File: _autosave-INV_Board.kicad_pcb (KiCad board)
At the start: 4 copper layers, 84 x 66.5 mm, 194 parts, among them J3 Conn_01x06_Male, J4 Conn_01x06_Female, J5 Conn_01x08_Female, J6 Conn_01x08_Female, J7 Conn_01x05_Male, J8 Conn_01x02_Male, Q1 2N7002, Q2 AO3401A, Q3 CRSS037N10N, Q4 CRSS037N10N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

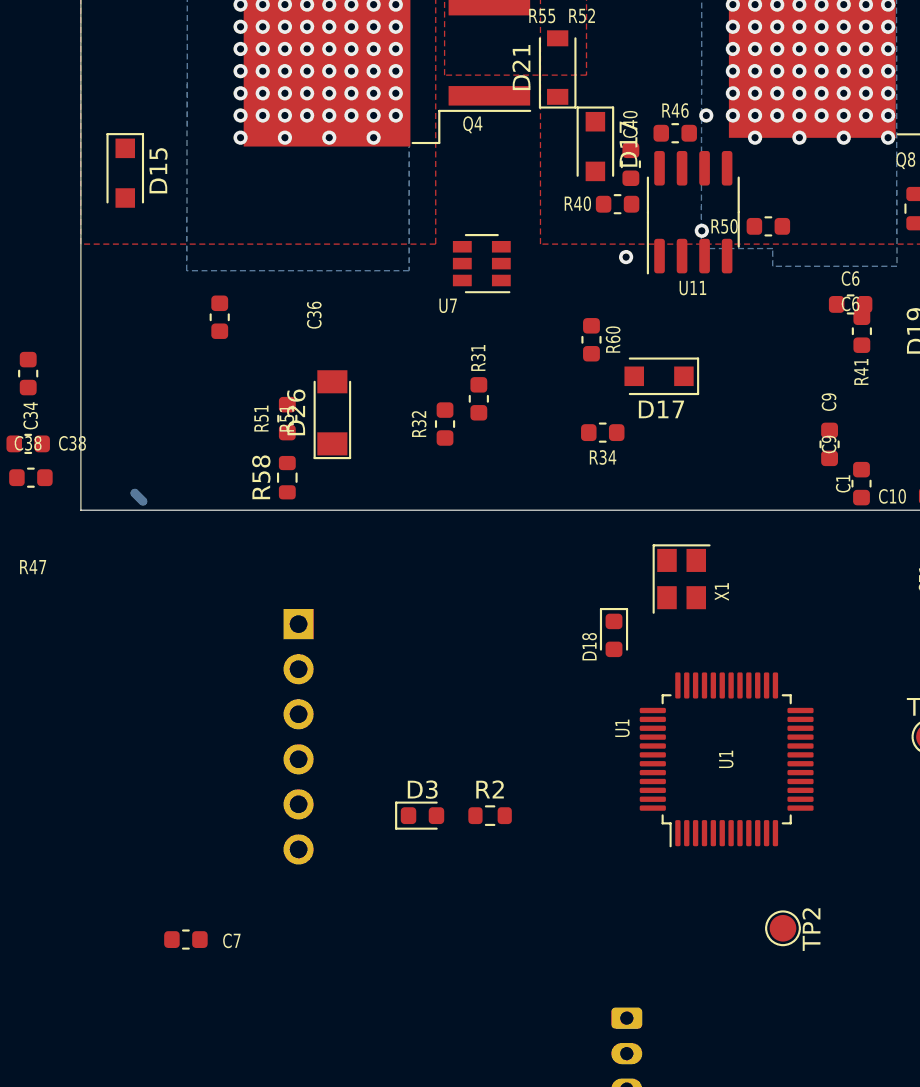
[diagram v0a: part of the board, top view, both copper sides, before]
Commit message: Checkpoint before deleting MCU ISense
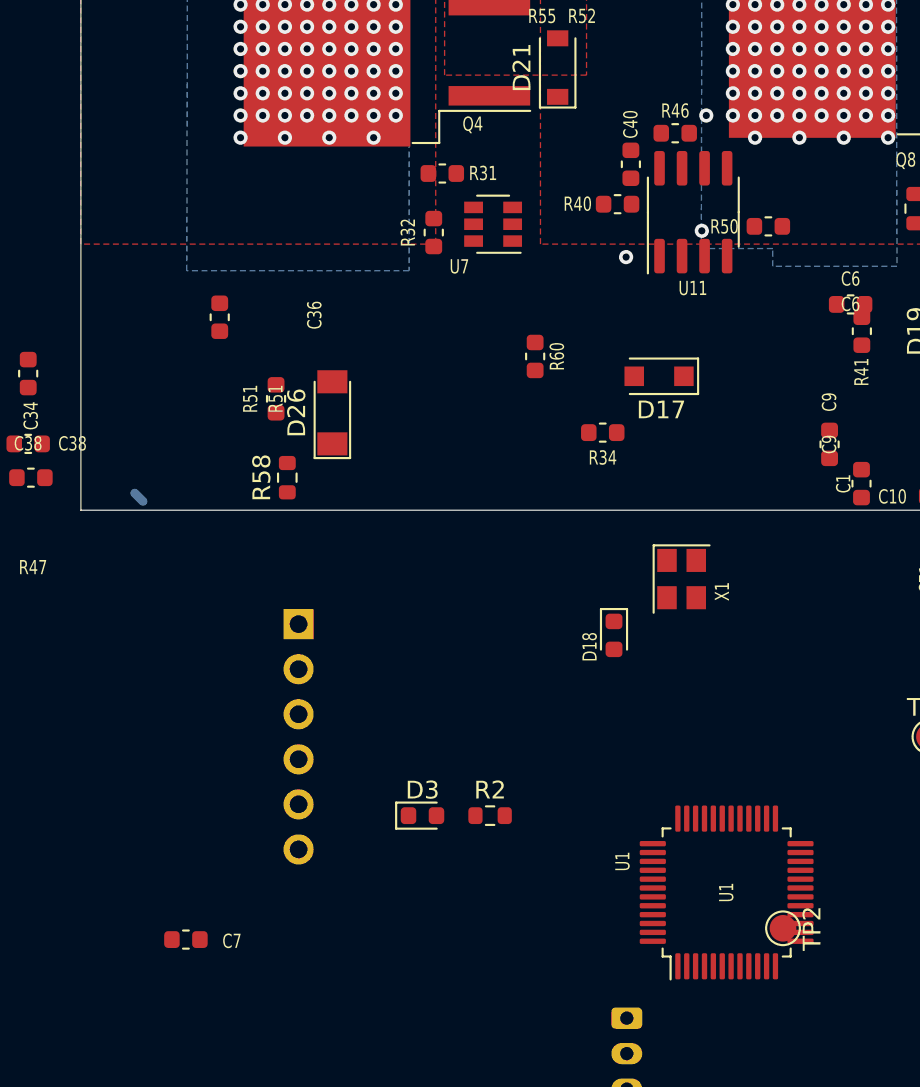
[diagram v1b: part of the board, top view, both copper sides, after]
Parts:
- removed the D15 at (118.5, 96.5)
- removed the D17 at (145.0, 95.0)
- moved R31 12.9 mm to (136.4, 96.5), turned to 0 degrees
- moved R32 10.8 mm to (135.9, 99.8)
- moved U1 7.50 mm to (152.4, 137.0)
- moved R60 3.31 mm to (141.6, 106.8)
- moved U7 2.31 mm to (139.2, 99.4)
- moved R51 1.29 mm to (127.0, 109.2)
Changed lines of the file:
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@@
   )
   (footprint "Package_QFP:LQFP-48_7x7mm_P0.5mm" (layer "F.Cu")
-    (at 152.4 129.54 90)
+    (at 152.4 137.045 90)
     (descr "LQFP, 48 Pin (https://www.analog.com/media/en/technical-documentation/data-sheets/ltc2358-16.pdf), generated with kicad-footprint-generator ipc_gullwing_generator.py")
     (tags "LQFP QFP")
@@
     )
   )
-  (footprint "Diode_SMD:D_SOD-123F" (layer "F.Cu")
-    (at 145 95 -90)
-    (descr "D_SOD-123F")
-    (tags "D_SOD-123F")
-    (property "LCSC" "C64898")
-    (property "Mouser Part no." "")
-    (property "MouserAlt" "")
-    (property "Sheetfile" "/Users/user/Documents/Git/my_MESC/INV_Board.sch")
-    (property "Sheetname" "")
-    (attr smd)
-    (fp_text reference "D17" (at -0.127 -1.905 -90) (layer "F.SilkS")
-      (effects (font (size 1 1) (thickness 0.15)))
-    )
-    (fp_text value "D_Sch_100V_2A" (at 0 2.1 -90) (layer "F.Fab")
-      (effects (font (size 1 1) (thickness 0.15)))
-    )
-    (fp_text user "${REFERENCE}" (at -0.127 -1.905 -90) (layer "F.Fab")
-      (effects (font (size 1 1) (thickness 0.15)))
-    )
-    (fp_line (start -2.2 1) (end 1.65 1) (layer "F.SilkS") (width 0.12))
-    (fp_line (start -2.2 -1) (end -2.2 1) (layer "F.SilkS") (width 0.12))
-    (fp_line (start -2.2 -1) (end 1.65 -1) (layer "F.SilkS") (width 0.12))
-    (fp_line (start 2.2 1.15) (end -2.2 1.15) (layer "F.CrtYd") (width 0.05))
-    (fp_line (start 2.2 -1.15) (end 2.2 1.15) (layer "F.CrtYd") (width 0.05))
-    (fp_line (start -2.2 -1.15) (end 2.2 -1.15) (layer "F.CrtYd") (width 0.05))
-    (fp_line (start -2.2 -1.15) (end -2.2 1.15) (layer "F.CrtYd") (width 0.05))
-    (fp_line (start -0.35 0) (end -0.35 0.55) (layer "F.Fab") (width 0.1))
-    (fp_line (start -0.35 0) (end -0.35 -0.55) (layer "F.Fab") (width 0.1))
-    (fp_line (start 1.4 -0.9) (end 1.4 0.9) (layer "F.Fab") (width 0.1))
-    (fp_line (start 0.25 -0.4) (end 0.25 0.4) (layer "F.Fab") (width 0.1))
-    (fp_line (start -1.4 -0.9) (end 1.4 -0.9) (layer "F.Fab") (width 0.1))
-    (fp_line (start 1.4 0.9) (end -1.4 0.9) (layer "F.Fab") (width 0.1))
-    (fp_line (start 0.25 0.4) (end -0.35 0) (layer "F.Fab") (width 0.1))
-    (fp_line (start -0.75 0) (end -0.35 0) (layer "F.Fab") (width 0.1))
-    (fp_line (start -0.35 0) (end 0.25 -0.4) (layer "F.Fab") (width 0.1))
-    (fp_line (start -1.4 0.9) (end -1.4 -0.9) (layer "F.Fab") (width 0.1))
-    (fp_line (start 0.25 0) (end 0.75 0) (layer "F.Fab") (width 0.1))
-    (pad "1" smd rect (at -1.4 0 270) (size 1.1 1.1) (layers "F.Cu" "F.Paste" "F.Mask")
-      (net 52 "Net-(C40-Pad1)") (pinfunction "K") (pintype "passive"))
-    (pad "2" smd rect (at 1.4 0 270) (size 1.1 1.1) (layers "F.Cu" "F.Paste" "F.Mask")
-      (net 62 "Net-(D17-Pad2)") (pinfunction "A") (pintype "passive"))
-    (model "${KICAD6_3DMODEL_DIR}/Diode_SMD.3dshapes/D_SOD-123F.wrl"
-      (offset (xyz 0 0 0))
-      (scale (xyz 1 1 1))
-      (rotate (xyz 0 0 0))
-    )
-  )
-  (footprint "Diode_SMD:D_SOD-123F" (layer "F.Cu")
-    (at 118.5 96.5 -90)
-    (descr "D_SOD-123F")
-    (tags "D_SOD-123F")
-    (property "LCSC" "C64898")
-    (property "Mouser Part no." "")
-    (property "MouserAlt" "")
-    (property "Sheetfile" "/Users/user/Documents/Git/my_MESC/INV_Board.sch")
-    (property "Sheetname" "")
-    (attr smd)
-    (fp_text reference "D15" (at -0.127 -1.905 -90) (layer "F.SilkS")
-      (effects (font (size 1 1) (thickness 0.15)))
-    )
-    (fp_text value "D_Sch_100V_2A" (at 0 2.1 -90) (layer "F.Fab")
-      (effects (font (size 1 1) (thickness 0.15)))
-    )
-    (fp_text user "${REFERENCE}" (at -0.127 -1.905 -90) (layer "F.Fab")
-      (effects (font (size 1 1) (thickness 0.15)))
-    )
-    (fp_line (start -2.2 -1) (end 1.65 -1) (layer "F.SilkS") (width 0.12))
-    (fp_line (start -2.2 -1) (end -2.2 1) (layer "F.SilkS") (width 0.12))
-    (fp_line (start -2.2 1) (end 1.65 1) (layer "F.SilkS") (width 0.12))
-    (fp_line (start -2.2 -1.15) (end 2.2 -1.15) (layer "F.CrtYd") (width 0.05))
-    (fp_line (start -2.2 -1.15) (end -2.2 1.15) (layer "F.CrtYd") (width 0.05))
-    (fp_line (start 2.2 1.15) (end -2.2 1.15) (layer "F.CrtYd") (width 0.05))
-    (fp_line (start 2.2 -1.15) (end 2.2 1.15) (layer "F.CrtYd") (width 0.05))
-    (fp_line (start 0.25 -0.4) (end 0.25 0.4) (layer "F.Fab") (width 0.1))
-    (fp_line (start -1.4 0.9) (end -1.4 -0.9) (layer "F.Fab") (width 0.1))
-    (fp_line (start 0.25 0.4) (end -0.35 0) (layer "F.Fab") (width 0.1))
-    (fp_line (start -0.35 0) (end 0.25 -0.4) (layer "F.Fab") (width 0.1))
-    (fp_line (start -1.4 -0.9) (end 1.4 -0.9) (layer "F.Fab") (width 0.1))
-    (fp_line (start -0.35 0) (end -0.35 0.55) (layer "F.Fab") (width 0.1))
-    (fp_line (start 1.4 0.9) (end -1.4 0.9) (layer "F.Fab") (width 0.1))
-    (fp_line (start -0.35 0) (end -0.35 -0.55) (layer "F.Fab") (width 0.1))
-    (fp_line (start 1.4 -0.9) (end 1.4 0.9) (layer "F.Fab") (width 0.1))
-    (fp_line (start -0.75 0) (end -0.35 0) (layer "F.Fab") (width 0.1))
-    (fp_line (start 0.25 0) (end 0.75 0) (layer "F.Fab") (width 0.1))
-    (pad "1" smd rect (at -1.4 0 270) (size 1.1 1.1) (layers "F.Cu" "F.Paste" "F.Mask")
-      (net 45 "Net-(C38-Pad1)") (pinfunction "K") (pintype "passive"))
-    (pad "2" smd rect (at 1.4 0 270) (size 1.1 1.1) (layers "F.Cu" "F.Paste" "F.Mask")
-      (net 60 "Net-(D15-Pad2)") (pinfunction "A") (pintype "passive"))
-    (model "${KICAD6_3DMODEL_DIR}/Diode_SMD.3dshapes/D_SOD-123F.wrl"
-      (offset (xyz 0 0 0))
-      (scale (xyz 1 1 1))
-      (rotate (xyz 0 0 0))
-    )
-  )
   (footprint "Package_TO_SOT_SMD:TO-263-2" (layer "F.Cu")
     (at 187.46 89.11 180)
@@
   )
   (footprint "Resistor_SMD:R_0603_1608Metric" (layer "F.Cu")
-    (at 144.78 105.8925 90)
+    (at 141.605 106.8325 90)
     (descr "Resistor SMD 0603 (1608 Metric), square (rectangular) end terminal, IPC_7351 nominal, (Body size source: http://www.tortai-tech.com/upload/download/2011102023233369053.pdf), generated with kicad-footprint-generator")
     (tags "resistor")
@@
   )
   (footprint "Resistor_SMD:R_0603_1608Metric" (layer "F.Cu")
-    (at 127.635 110.3375 90)
+    (at 127 109.22 90)
     (descr "Resistor SMD 0603 (1608 Metric), square (rectangular) end terminal, IPC_7351 nominal, (Body size source: http://www.tortai-tech.com/upload/download/2011102023233369053.pdf), generated with kicad-footprint-generator")
     (tags "resistor")
@@
   )
   (footprint "Package_TO_SOT_SMD:SOT-23-6" (layer "F.Cu")
-    (at 138.6 101.6 180)
+    (at 139.235 99.38 180)
     (descr "6-pin SOT-23 package")
     (tags "SOT-23-6")
@@
   )
   (footprint "Resistor_SMD:R_0603_1608Metric" (layer "F.Cu")
-    (at 138.43 109.22 90)
+    (at 136.3725 96.52)
     (descr "Resistor SMD 0603 (1608 Metric), square (rectangular) end terminal, IPC_7351 nominal, (Body size source: http://www.tortai-tech.com/upload/download/2011102023233369053.pdf), generated with kicad-footprint-generator")
     (tags "resistor")
@@
     (property "Sheetname" "")
     (attr smd)
-    (fp_text reference "R31" (at 2.3 0 90) (layer "F.SilkS")
+    (fp_text reference "R31" (at 2.3 0) (layer "F.SilkS")
       (effects (font (size 0.8 0.6) (thickness 0.12)))
     )
-    (fp_text value "R_30K" (at 0 1.43 90) (layer "F.Fab")
+    (fp_text value "R_30K" (at 0 1.43) (layer "F.Fab")
       (effects (font (size 1 1) (thickness 0.15)))
     )
-    (fp_text user "${REFERENCE}" (at 0 0 90) (layer "F.Fab")
+    (fp_text user "${REFERENCE}" (at 0 0) (layer "F.Fab")
       (effects (font (size 0.8 0.6) (thickness 0.12)))
     )
@@
     (fp_line (start 0.8 -0.4) (end 0.8 0.4) (layer "F.Fab") (width 0.1))
     (fp_line (start -0.8 0.4) (end -0.8 -0.4) (layer "F.Fab") (width 0.1))
-    (pad "1" smd roundrect locked (at -0.7875 0 90) (size 0.875 0.95) (layers "F.Cu" "F.Paste" "F.Mask") (roundrect_rratio 0.25)
+    (pad "1" smd roundrect locked (at -0.7875 0) (size 0.875 0.95) (layers "F.Cu" "F.Paste" "F.Mask") (roundrect_rratio 0.25)
       (net 92 "Net-(R31-Pad1)") (pintype "passive"))
-    (pad "2" smd roundrect locked (at 0.7875 0 90) (size 0.875 0.95) (layers "F.Cu" "F.Paste" "F.Mask") (roundrect_rratio 0.25)
+    (pad "2" smd roundrect locked (at 0.7875 0) (size 0.875 0.95) (layers "F.Cu" "F.Paste" "F.Mask") (roundrect_rratio 0.25)
       (net 79 "SGU") (pintype "passive"))
     (model "${KISYS3DMOD}/Resistor_SMD.3dshapes/R_0603_1608Metric.wrl"
@@
   )
   (footprint "Resistor_SMD:R_0603_1608Metric" (layer "F.Cu")
-    (at 136.525 110.6425 90)
+    (at 135.89 99.8475 90)
     (descr "Resistor SMD 0603 (1608 Metric), square (rectangular) end terminal, IPC_7351 nominal, (Body size source: http://www.tortai-tech.com/upload/download/2011102023233369053.pdf), generated with kicad-footprint-generator")
     (tags "resistor")

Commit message: Save progress
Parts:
- removed C49: CP_470uF+, Capacitor_THT:CP_Radial_D16.0mm_P7.50mm
- removed C63, C65, C66: C_0.1uF_100V, Capacitor_SMD:C_0603_1608Metric
- removed D18: D_TVS, Diode_SMD:D_0603_1608Metric
- removed R59, R61, R63: R_4k7, Resistor_SMD:R_0603_1608Metric
- removed R60, R62, R64: R_150, Resistor_SMD:R_0603_1608Metric
- removed TP1, TP2, TP3: TestPoint, TestPoint:TestPoint_Pad_D1.5mm
- added U12: SMF05CT1G, Package_TO_SOT_SMD:SOT-363_SC-70-6, F.Cu at (190.8, 104.6)
- added U13: SMF05CT1G, Package_TO_SOT_SMD:SOT-363_SC-70-6, F.Cu at (172.2, 127.8)
- added U14: SMF05CT1G, Package_TO_SOT_SMD:SOT-363_SC-70-6, F.Cu at (151.6, 124.5)
- J4, J5, J7: moved to F.Cu
- R1: footprint Resistor_SMD:R_0805_2012Metric -> Resistor_SMD:R_0603_1608Metric
- X1: footprint Oscillator:Oscillator_SMD_Abracon_ASE-4Pin_3.2x2.5mm -> INV_Board:X1OSC
- moved J6 152.7 mm to (196.2, 132.7), turned to 90 degrees
- moved C14 141.7 mm to (191.3, 132.1), turned to 180 degrees
- moved C15 140.8 mm to (191.3, 129.8), turned to 180 degrees
- moved R9 138.0 mm to (191.3, 126.7), turned to 180 degrees
- moved R8 137.2 mm to (187.5, 133.3), turned to 0 degrees
- moved C11 133.5 mm to (187.4, 131.3), turned to 180 degrees
- moved C12 132.6 mm to (187.4, 129.3), turned to 180 degrees
- moved C5 123.5 mm to (187.5, 127.3), turned to 0 degrees
- moved R1 121.6 mm to (191.8, 122.7)
- moved Q1 121.5 mm to (182.2, 122.7)
- moved Q2 120.7 mm to (187.3, 123.1)
- moved U2 116.8 mm to (179.6, 128.5), turned to 180 degrees
- moved J4 110.9 mm to (197.4, 103.5), turned to -90 degrees
- moved C21 99.8 mm to (118.9, 114.8)
- moved U5 97.3 mm to (123.4, 114.8)
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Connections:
- J5 pad 7: I2CSDA -> I2CSCL
- R20 pad 2: Net-(J7-Pad3) -> Net-(J7-Pad2)
- R21 pad 2: I2CSDA -> I2CSCL
- R27 pad 2: Net-(J7-Pad2) -> Net-(J7-Pad3)
- U1 pad 11: ISU_MCU -> unconnected-(U1-Pad11)
- U1 pad 17: ISV_MCU -> unconnected-(U1-Pad17)
- U1 pad 18: ISW_MCU -> unconnected-(U1-Pad18)
- U1 pad 46: I2CSDA -> I2CSCL
- U5 pad 9: (no net) -> SGU
- U8 pad 9: (no net) -> SGU
- X1 pad 2: GND -> SGU
- X1 pad 3: Net-(U2-Pad5) -> Net-(U1-Pad5)
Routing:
- net +12V: track 0.65 -> 176.1 mm, vias 0 -> 6
- net SGU: track 0.00 -> 36.3 mm, vias 104 -> 108
- net ISW: track 0.00 -> 28.9 mm, vias 0 -> 2
- net /VGH: track 0.00 -> 24.1 mm
- net Net-(R45-Pad1): track 0.00 -> 23.4 mm, vias 0 -> 2
- net /VGL: track 0.00 -> 22.2 mm, vias 1 -> 2
- net /WGL: track 0.00 -> 20.0 mm, vias 0 -> 2
- net +VDC: track 10.5 -> 24.2 mm, vias 177 -> 194
- net Net-(C8-Pad1): track 0.00 -> 12.0 mm, vias 0 -> 2
- net SWW: track 0.00 -> 11.9 mm
- net PhaseW: track 0.00 -> 11.9 mm
- net Net-(R3-Pad2): track 0.00 -> 9.21 mm
- net SWV: track 0.00 -> 7.48 mm
- net /WGH: track 0.00 -> 7.29 mm
- net Net-(C38-Pad1): track 0.00 -> 6.32 mm
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- added copper zone on F.Cu, net +12V
- added copper zone on F.Cu, net Net-(C8-Pad2)
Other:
- board size 84 x 66.5 mm -> 84.1 x 87.1 mm
- board text removed: "#Res N/C SWO SWC SWDIO G"
- board text removed: "3v3"
- board text removed: "5V 3V3 G An Rx Tx An An"
- board text removed: "G 5V PWM"
- board text removed: "G H3 H2 H1 N/C 5V"
- board text removed: "I_PhU TP"
- board text removed: "I_PhV TP"
- board text removed: "I_PhW TP"
- board text removed: "PhU"
- board text removed: "PhV"
- board text removed: "PhW"
- board text removed: "SDA SCL 3v3 G"
- board text removed: "USB B Micro"
